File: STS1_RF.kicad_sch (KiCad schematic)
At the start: 83 parts, among them J1 UHF, Q1 SQ2318, Q3 SQ2318, Q4 SQ2318, U10 TQP3M9036, U11 74LVC1G14Z-7, U16 F2972, U2 LP2985-1.8, U30 TMP36xS, U4 74LVC2G74, U5 TYKTBCSANF-26.000000, U8 Si4463, U9 LFCG-490+

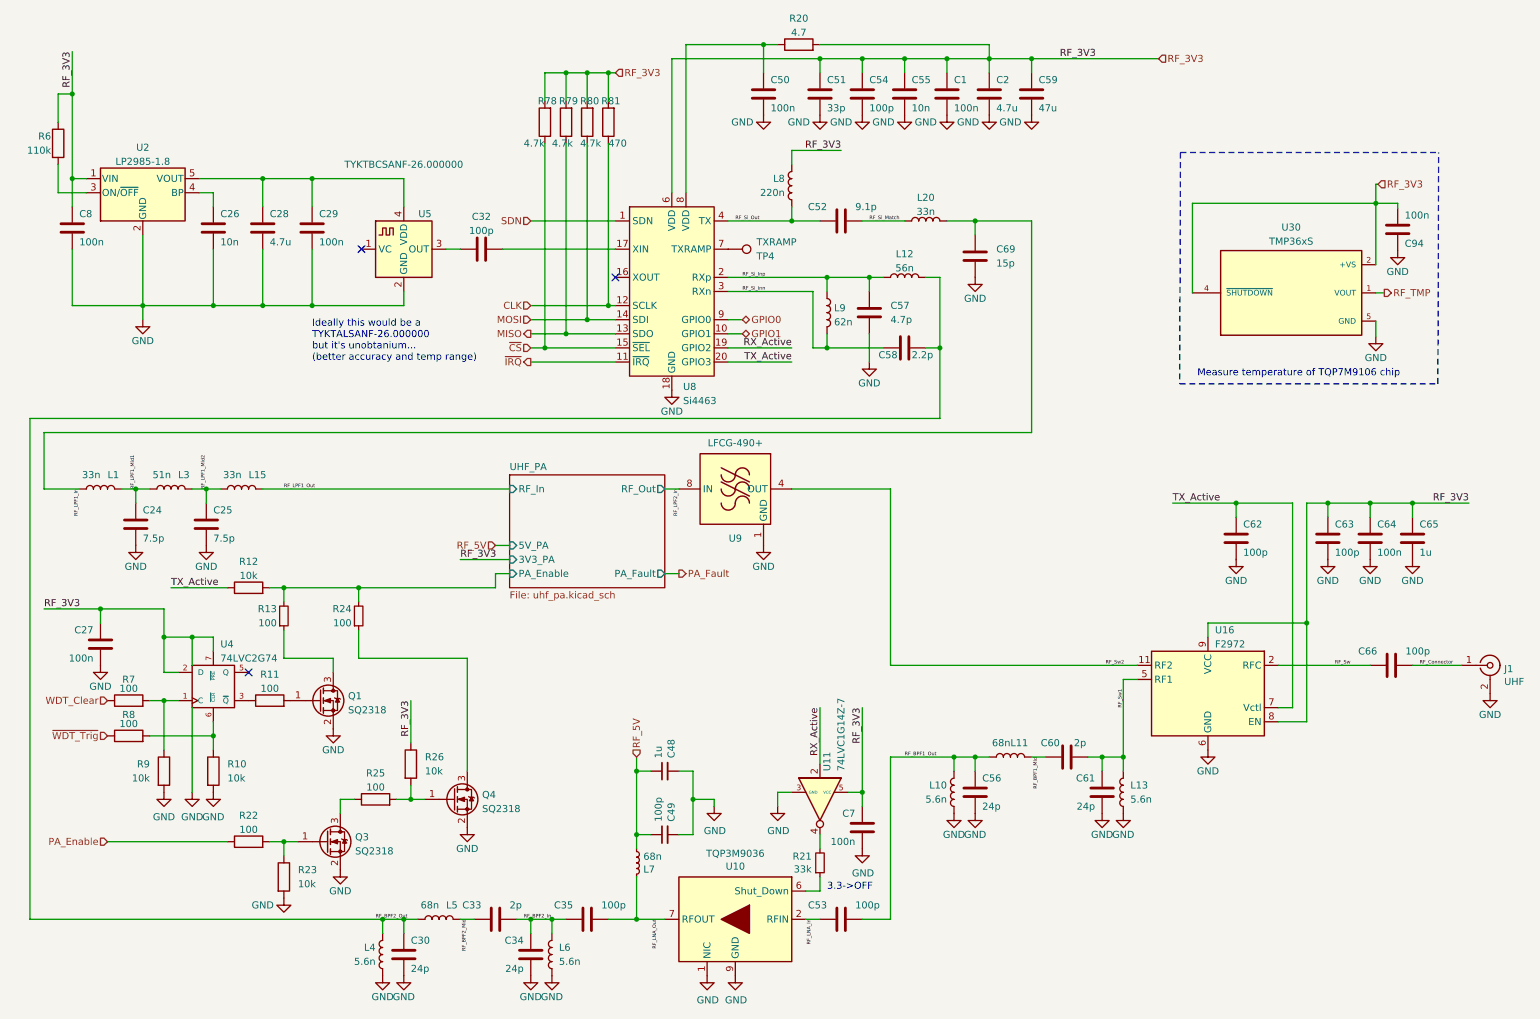
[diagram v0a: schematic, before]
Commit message: fix: use 0805 size inductor for PA power supply and make DRC happy after KiCAD10 upgrade
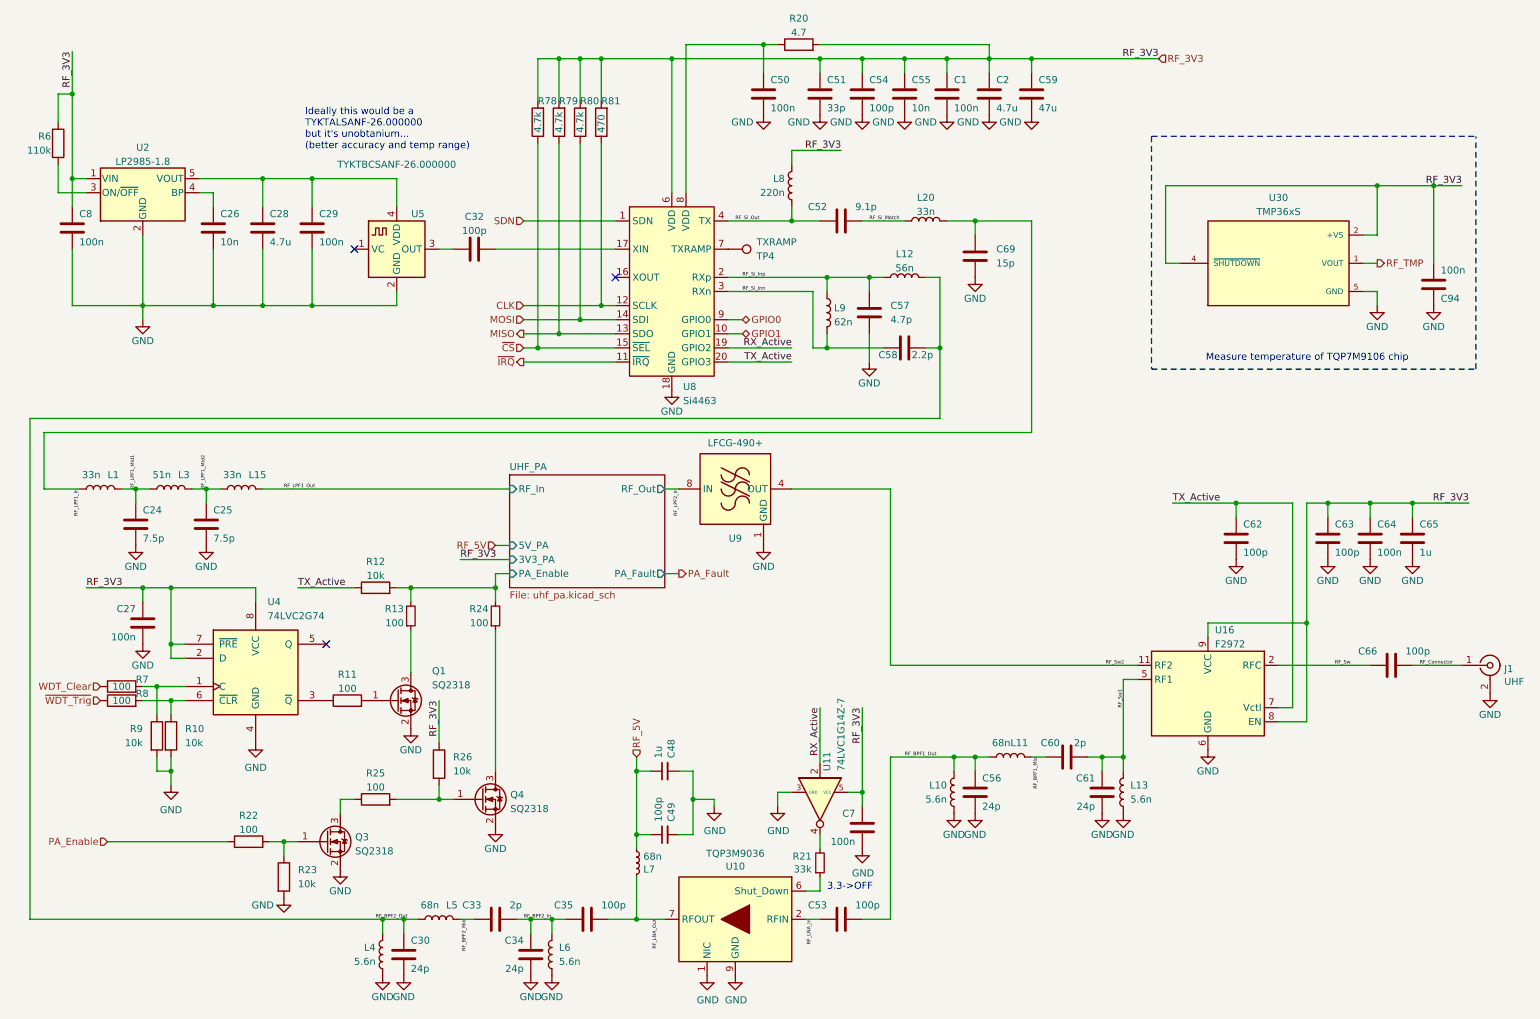
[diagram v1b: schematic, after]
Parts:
- U4: footprint Package_SO:VSSOP-8_2.4x2.1mm_P0.5mm -> Package_SO:VSSOP-8_2.3x2mm_P0.5mm
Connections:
- net VCC renamed RF_3V3
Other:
- moved on the sheet: C27, C32, C94, Q1, Q4, R10, R11, R12, R13, R24, R26, R7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
